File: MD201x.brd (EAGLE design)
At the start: 80 x 50 mm, 103 parts, among them IC1 78L05F, IC2 LM321MF, J1 8P8C-LED, J10 1744446-4, J2 1744446-4, J3 XH-4-SIDE, J4 MA04-2, J5 MA05-2, J6 MA02-2, Q1 N-MOSFET-, Q2 N-MOSFET-, Q3 N-MOSFET-, Q4 N-MOSFET-, U1 STM32F103C8, U10 XC6206, U11 74AHC1G08DCK, U12 74AHC1G08DCK, U13 74AHC1G08DCK, U14 74AHC1G08DCK, U15 74AHC1G08DCK, U2 NCV7351D1E, U3 SI8621AB-B-IS, U4 TLP184, U5 NCP5106D, U6 NCP5106D, U7 NCS199, U8 7815DT, U9 7805DT, X1 CSTCE8M00G55

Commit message: 横向き
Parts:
- removed C35: 22u, rcl:E2,5-5
- removed U11, U12, U13, U14, U15: 74AHC1G08DCK, 74xx-little-us:SC70-5
- added D2, D3, D5, D6: (no value), diode:SOD523
- added Q5: BSS123, transistor-small-signal:SOT23
- added R19: 0.5m, r_shunt:CSS2H-2512
- C33: device rcl:C0805 -> rcl:C0603
- C36: device rcl:C0603 -> rcl:C1210
- U$1: value XT60PW -> XT60PW-M; device lib_ysk:XT60PW-F -> lib_ysk:XT60PW-M
- U$2: value XT60PW -> XT60PW-F
- moved R17 101.6 mm to (20.1, 47.5), flipped to the bottom
- moved R18 94.9 mm to (20.1, 34.8), flipped to the bottom
- moved D1 43.1 mm to (62.4, -2.26), turned to 270 degrees
- moved C15 40.8 mm to (34.1, 46.1)
- moved U7 36.5 mm to (45.0, 44.5), flipped to the top, turned to 270 degrees
- moved C27 36.3 mm to (34.0, -4.16), turned to 90 degrees
- moved C28 33.0 mm to (40.4, -3.50), turned to 90 degrees
- moved C11 32.4 mm to (48.3, 8.88), flipped to the bottom, turned to 0 degrees
- moved C13 31.2 mm to (50.2, 7.51), flipped to the top, turned to 0 degrees
- moved R3 28.6 mm to (68.8, 41.9)
- moved C5 27.5 mm to (49.7, 11.9), flipped to the bottom, turned to 0 degrees
- moved D4 25.9 mm to (59.3, -2.70), turned to 270 degrees
- moved R5 24.7 mm to (68.2, 43.9)
- moved C36 24.6 mm to (14.1, 42.1), flipped to the bottom, turned to 180 degrees
- moved IC1 24.4 mm to (14.6, 46.8), flipped to the bottom, turned to 90 degrees
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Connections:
- net N$23 renamed CANTX_ISO
- net N$27 renamed CANRX_ISO
- net VCS_N renamed VCS_B_N
- net VCS_P renamed VCS_B_P
- removed net 24V_ISO: C35.+, C36.1, IC1.3, J1.4, J1.5, R20.1
- removed net VCS: C11.2, C12.2, C5.2, C6.2, Q2.1, Q2.2, Q2.3, Q4.1, Q4.2, Q4.3, R7.1, R8.1, R9.2$1, R9.2$2
- new net A_LS: Q2.1, Q2.2, Q2.3, R19.2, R7.1
- new net B_LS: C6.2, Q4.1, Q4.2, Q4.3, R8.1, R9.2
- new net DC_ISO: C36.1, IC1.3, J1.4, J1.5, R20.1
- new net ISENSE_B: C16.2, R123.1
- new net N$13: J6.1
- net !EMS: no longer U12.1, U13.1, U14.1, U15.1
- net +3V3: no longer U12.5, U13.5, U14.5, U15.5
- net 5V_ISO: now also R17.2; no longer U11.5
- net CANH: no longer J6.1
- net CANL: no longer R12.1
- net GNDA: now also C11.2, C12.2, C5.2, R19.1, R9.1; no longer R9.1$1, R9.1$2, U12.3, U13.3, U14.3, U15.3
- net GNDIO: now also Q5.2; no longer C35.-, R17.1, U11.3
- net IN_HI_A: no longer U13.4
- net IN_HI_A_PRE: no longer U13.2
- net IN_HI_B: no longer U14.4
- net IN_HI_B_PRE: no longer U14.2
- net IN_LO_A: no longer U12.4
- net IN_LO_A_PRE: no longer U12.2
- net IN_LO_B: no longer U15.4
- net IN_LO_B_PRE: no longer U15.2
- net ISENSE: no longer C16.2, R123.1
- net N$1: now also D6.C
- net N$11: now also D5.C
- net N$12: now also D2.A
- net N$16: now also R17.1; no longer U11.4
- net N$17: now also Q5.3; no longer R17.2
- net N$2: now also D2.C
- net N$4: now also D6.A
- net N$5: now also D3.C
- net N$61: now also D5.A
- net N$64: now also D3.A
- net N$8: now also Q5.1; no longer U11.1, U11.2
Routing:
- net +3V3: track 85.9 -> 34.6 mm, vias 6 -> 2
- net DC_ISO: track 0.00 -> 27.6 mm, vias 0 -> 2
- net SWDIO: track 29.5 -> 4.91 mm, vias 1 -> 0
- net SWCLK: track 23.6 -> 5.09 mm, vias 1 -> 0
- net 3V3A: track 25.9 -> 7.83 mm
- net 24V_ISO: track 17.4 -> 0.00 mm
- net UART_TX: track 18.3 -> 2.51 mm, vias 1 -> 0
- net UART_RX: track 20.3 -> 4.73 mm, vias 1 -> 0
- net N$67: track 14.8 -> 0.00 mm
- net N$5: track 13.2 -> 0.00 mm, vias 1 -> 0
- net B_OUT: track 28.4 -> 15.8 mm, vias 1 -> 0
- net !EMS: track 25.7 -> 16.8 mm, vias 2 -> 1
- net N$2: track 11.6 -> 2.94 mm, vias 1 -> 0
- net N$17: track 0.00 -> 7.31 mm
- net N$64: track 5.50 -> 0.00 mm
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- added copper zone on layer 16, net A_LS
- added copper zone on layer 16, net B_LS
- added copper zone on layer 16, net B_OUT
- removed copper zone on layer 1, net A_OUT
- removed copper zone on layer 1, net B_OUT
- removed copper zone on layer 1, net VCS
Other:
- board text removed: "0"
- board text removed: "1"
- board text removed: "2"
- board text removed: "3"
- board text removed: "4"
- board text removed: "CAN TERM."
- board text removed: "OPEN"
- board text removed: "TERM"

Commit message: staging everything i have right now
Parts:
- removed U7: NCS199, on-semi:SOT65P210X110-6
- added C31: (no value), rcl:C0603
- added CN2: (no value), jst-xa:S3B-XASK-1
- added R22, R23: 10, rcl:R0603
- added U$3: INA186DCK, lib_ysk:SOT65P210X110-6
- U5: value NCP5106D -> NCP5106MN; device on-semi:SOIC127P600X175-8 -> on-semi:SON80P400X400X100-11T275X300
- U6: value NCP5106D -> NCP5106; device on-semi:SOIC127P600X175-8 -> on-semi:SO08
- moved D5 122.4 mm to (50.4, 20.3), flipped to the bottom, turned to 180 degrees
- moved D3 121.2 mm to (40.7, 32.6), turned to 90 degrees
- moved CN1 74.5 mm to (16.4, 9.40), turned to 180 degrees
- moved D6 62.7 mm to (-7.40, -11.7)
- moved R7 42.4 mm to (40.9, 12.4)
- moved D4 40.5 mm to (34.4, 29.3), flipped to the top, turned to 180 degrees
- moved U5 38.0 mm to (39.6, 11.9), flipped to the top, turned to 0 degrees
- moved J2 32.3 mm to (48.7, -16.1)
- moved C1 32.0 mm to (58.4, 43.8), turned to 90 degrees
- moved C22 31.9 mm to (-14.8, 19.9)
- moved C2 30.9 mm to (48.0, 43.8), turned to 90 degrees
- moved R3 29.7 mm to (50.5, 18.5)
- moved S1 27.3 mm to (-10.0, 16.3)
- moved R6 26.8 mm to (42.0, 23.0), turned to 90 degrees
- moved J10 18.2 mm to (4.50, -4.40)
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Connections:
- new net 0V: C11.2, C12.2, C5.2, R19.1, R9.1
- new net N$15: C31.2, R22.2, U$3.5
- new net N$22: C31.1, R23.2, U$3.4
- net 3V3A: now also U$3.3; no longer U7.3
- net GNDA: now also U$3.2; no longer C11.2, C12.2, C5.2, R19.1, R9.1, U7.2
- net N$1: now also U5.8; no longer U5.7
- net N$6: no longer U7.6
- net N$73: now also U5.10; no longer U5.8
- net REF: no longer U7.1
- net VCS_B_N: now also R22.1; no longer U7.5
- net VCS_B_P: now also R23.1; no longer U7.4
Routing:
- net +5V: track 40.8 -> 30.3 mm
- net N$11: track 0.00 -> 10.3 mm
- net !RESET: track 14.7 -> 5.97 mm, vias 1 -> 0
- net N$64: track 0.00 -> 7.88 mm
- net N$12: track 9.49 -> 15.4 mm
- net DC_ISO: track 27.6 -> 22.0 mm
- net SWCLK: track 5.09 -> 0.00 mm
- net SWDIO: track 4.91 -> 0.00 mm
- net UART_RX: track 4.73 -> 0.00 mm
- net N$61: track 0.00 -> 3.76 mm
- net VCS_B_N: track 0.00 -> 3.68 mm
- net +3V3: track 34.6 -> 31.0 mm
- net N$2: track 2.94 -> 0.00 mm
- net !EMS_ISO: track 9.58 -> 6.65 mm
- net UART_TX: track 2.51 -> 0.00 mm
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- added copper zone on layer 1, net 0V
- added copper zone on layer 16, net 0V

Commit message: idk
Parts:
- removed J10, J2: 1744446-4, con-ep25:1744446-4
- removed J3: XH-4-SIDE, con-xh:CON-XH-4-SIDE
- moved C31 3.44 mm to (41.6, 28.3), turned to 180 degrees
- moved R23 1.94 mm to (40.6, 30.9), turned to 270 degrees
- moved R22 1.12 mm to (42.7, 30.9), turned to 270 degrees
- moved U$3 1.08 mm to (38.1, 30.4), turned to 270 degrees
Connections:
- new net CS_OUT_A: U$3.6
- new net CS_REF: U$3.1
- net +5V: no longer J10.P2, J3.P$2
- net ENC_A: no longer J10.P3
- net ENC_B: no longer J10.P4
- net GNDA: no longer J10.P1, J3.P$1
- net IN_A: no longer J3.P$3
- net IN_B: no longer J3.P$4
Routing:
- net VCS_B_P: track 7.89 -> 10.4 mm
- net N$15: track 0.00 -> 1.85 mm
- net N$22: track 0.00 -> 1.81 mm
- net VCS_B_N: track 3.68 -> 2.56 mm

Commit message: stage everything
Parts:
- removed D4: BAS16W, diode:SOD323-R
- removed U6: NCP5106, on-semi:SO08
- added U$4: DGD05473FN, lib_ysk:SON50P300X300X80-11T165X260
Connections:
- net +15V: now also U$4.1; no longer D4.A, U6.1
- net B_OUT: now also U$4.5; no longer U6.6
- net GNDA: now also U$4.11, U$4.9; no longer U6.4
- net IN_HI_B: now also U$4.7; no longer U6.2
- net IN_LO_B: now also U$4.8; no longer U6.3
- net N$2: now also U$4.4; no longer U6.7
- net N$5: now also U$4.10; no longer U6.5
- net N$67: now also U$4.3; no longer D4.C, U6.8
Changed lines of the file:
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@@
 <attribute name="NAME" x="59.61" y="31.727" size="1.27" layer="26" font="vector" rot="MR90"/>
-</element>
-<element name="D4" library="diode" library_urn="urn:adsk.eagle:library:210" package="SOD323-R" package3d_urn="urn:adsk.eagle:package:43437/1" value="BAS16W" x="34.4" y="29.3" smashed="yes" rot="R180">
-<attribute name="NAME" x="34.151" y="28.121" size="1.27" layer="25" font="vector" rot="R90"/>
 </element>
 <element name="C10" library="rcl" package="C0603" value="100n/25V" x="34.4" y="26.9" smashed="yes">
@@
 <attribute name="VALUE" x="43.537" y="9.995" size="1.27" layer="27" rot="R90"/>
 </element>
-<element name="U6" library="on-semi" package="SO08" package3d_urn="urn:adsk.eagle:package:15356/1" value="NCP5106" x="39.4" y="25.3" smashed="yes" rot="R270">
-<attribute name="NAME" x="36.997" y="26.29" size="1.27" layer="25" font="vector" rot="SR270"/>
-<attribute name="VALUE" x="37.495" y="21.363" size="1.27" layer="27"/>
-</element>
 <element name="R9" library="r_shunt" package="CSS2H-2512" value="0.5m" x="47.8" y="30.6" smashed="yes" rot="MR180">
 <attribute name="NAME" x="46.449" y="31.122" size="1.27" layer="26" font="vector" rot="SMR180"/>
@@
 <attribute name="SPICEPREFIX" value="C" x="41.6" y="28.3" size="1.778" layer="28" rot="MR180" display="off"/>
 <attribute name="VALUE" x="40.965" y="30.205" size="1.27" layer="28" rot="MR180"/>
+</element>
+<element name="U$4" library="lib_ysk" package="SON50P300X300X80-11T165X260" package3d_urn="urn:adsk.eagle:package:12826382/1" value="DGD05473FN" x="41.7" y="27" smashed="yes">
+<attribute name="NAME" x="41.7" y="29.521" size="1.27" layer="25" align="bottom-center"/>
+<attribute name="VALUE" x="41.7" y="24.751" size="1.27" layer="27" align="top-center"/>
 </element>
 </elements>
@@
 <signal name="+15V">
 <contactref element="D1" pad="A"/>
-<contactref element="D4" pad="A"/>
-<contactref element="U6" pad="1"/>
 <contactref element="U5" pad="1"/>
 <contactref element="C7" pad="1"/>
@@
 <contactref element="U9" pad="1"/>
 <contactref element="C13" pad="1"/>
+<contactref element="U$4" pad="1"/>
 <wire x1="45.208" y1="56.034" x2="44.222" y2="59.569" width="0" layer="19" extent="1-1"/>
 <wire x1="37.82" y1="58.426" x2="44.222" y2="59.569" width="0" layer="19" extent="1-1"/>
 <wire x1="35.639" y1="33.173" x2="45.208" y2="56.034" width="0" layer="19" extent="16-16"/>
-<wire x1="33.3" y1="29.3" x2="35.639" y2="33.173" width="0" layer="19" extent="1-16"/>
-<wire x1="37.05" y1="27.205" x2="33.3" y2="29.3" width="0" layer="19" extent="1-1"/>
-<wire x1="37.64" y1="13.5" x2="37.05" y2="27.205" width="0" layer="19" extent="1-1"/>
+<wire x1="40.2654" y1="28" x2="35.639" y2="33.173" width="0" layer="19" extent="1-16"/>
+<wire x1="37.64" y1="13.5" x2="40.2654" y2="28" width="0" layer="19" extent="1-1"/>
 <wire x1="35" y1="13.05" x2="37.64" y2="13.5" width="0" layer="19" extent="1-16"/>
 <wire x1="46.278" y1="4.306" x2="37.64" y2="13.5" width="0" layer="19" extent="1-1"/>
@@
 <contactref element="U5" pad="4"/>
 <contactref element="C7" pad="2"/>
-<contactref element="U6" pad="4"/>
 <contactref element="C8" pad="2"/>
 <contactref element="U3" pad="4"/>
@@
 <contactref element="U$1" pad="NEG"/>
 <contactref element="U$3" pad="2"/>
+<contactref element="U$4" pad="9"/>
+<contactref element="U$4" pad="11"/>
 <wire x1="42.668" y1="56.034" x2="51.522" y2="61.849" width="0" layer="19" extent="1-1"/>
 <wire x1="33.818" y1="54.231" x2="42.668" y2="56.034" width="0" layer="19" extent="1-1"/>
@@
 <contactref element="Q3" pad="1"/>
 <contactref element="Q3" pad="2"/>
-<contactref element="U6" pad="6"/>
 <contactref element="R6" pad="1"/>
 <polygon width="0.1524" layer="16" thermals="no" rank="3">
@@
 <wire x1="44.1" y1="22.8" x2="43.3" y2="22" width="0.254" layer="16"/>
 <wire x1="49" y1="22.8" x2="44.1" y2="22.8" width="0.254" layer="16"/>
+<contactref element="U$4" pad="5"/>
 <wire x1="58.825" y1="27.505" x2="56.8" y2="31.6" width="0" layer="19" extent="16-16"/>
 <wire x1="42" y1="22.15" x2="43.3" y2="22" width="0" layer="19" extent="16-16"/>
-<wire x1="41.75" y1="24.665" x2="42" y2="22.15" width="0" layer="19" extent="1-16"/>
-<wire x1="35.25" y1="26.9" x2="41.75" y2="24.665" width="0" layer="19" extent="1-1"/>
+<wire x1="40.2654" y1="26" x2="42" y2="22.15" width="0" layer="19" extent="1-16"/>
+<wire x1="35.25" y1="26.9" x2="40.2654" y2="26" width="0" layer="19" extent="1-1"/>
 <wire x1="64" y1="13.4" x2="56.7" y2="22.2" width="0" layer="19" extent="16-16"/>
 </signal>
 <signal name="N$67">
-<contactref element="D4" pad="C"/>
 <contactref element="C10" pad="1"/>
-<contactref element="U6" pad="8"/>
-<wire x1="35.5" y1="29.3" x2="41.75" y2="27.205" width="0" layer="19" extent="1-1"/>
-<wire x1="33.55" y1="26.9" x2="35.5" y2="29.3" width="0" layer="19" extent="1-1"/>
+<contactref element="U$4" pad="3"/>
+<wire x1="33.55" y1="26.9" x2="40.2654" y2="27" width="0" layer="19" extent="1-1"/>
 </signal>
 <signal name="A_OUT">
@@
 <contactref element="R4" pad="1"/>
 <contactref element="R8" pad="2"/>
-<contactref element="U6" pad="5"/>
 <contactref element="D3" pad="C"/>
+<contactref element="U$4" pad="10"/>
 <wire x1="40.7" y1="32" x2="40.95" y2="35.3" width="0" layer="19" extent="1-1"/>
 <wire x1="42.4" y1="31.75" x2="40.7" y2="32" width="0" layer="19" extent="1-1"/>
-<wire x1="41.75" y1="23.395" x2="42.4" y2="31.75" width="0" layer="19" extent="1-1"/>
+<wire x1="43.1346" y1="28" x2="42.4" y2="31.75" width="0" layer="19" extent="1-1"/>
 </signal>
 <signal name="+3V3">
@@
 <contactref element="R2" pad="1"/>
 <contactref element="R6" pad="2"/>
-<contactref element="U6" pad="7"/>
 <contactref element="D2" pad="C"/>
-<wire x1="42" y1="23.85" x2="41.75" y2="25.935" width="0" layer="19" extent="1-16"/>
+<contactref element="U$4" pad="4"/>
 <wire x1="39.8" y1="23.85" x2="42" y2="23.85" width="0" layer="19" extent="16-16"/>
 <wire x1="37.8" y1="23.7" x2="39.8" y2="23.85" width="0" layer="19" extent="16-16"/>
+<wire x1="40.2654" y1="26.5" x2="39.8" y2="23.85" width="0" layer="19" extent="1-16"/>
 </signal>
 <signal name="CANH">
@@
 <wire x1="23.876" y1="25.312" x2="25.865" y2="45.443" width="0" layer="19" extent="16-16"/>
 <wire x1="25.306021875" y1="19.05" x2="22.225" y2="20.955" width="0" layer="19" extent="1-1"/>
-</signal>
-<signal name="IN_HI_B">
-<contactref element="U6" pad="2"/>
 </signal>
 <signal name="GNDIO">
@@
 <contactref element="U5" pad="3"/>
 </signal>
-<signal name="IN_LO_B">
-<contactref element="U6" pad="3"/>
-</signal>
 <signal name="N$6">
 <contactref element="R123" pad="2"/>
@@
 <contactref element="U$3" pad="6"/>
 </signal>
+<signal name="IN_LO_B">
+<contactref element="U$4" pad="8"/>
+</signal>
+<signal name="IN_HI_B">
+<contactref element="U$4" pad="7"/>
+</signal>
 </signals>

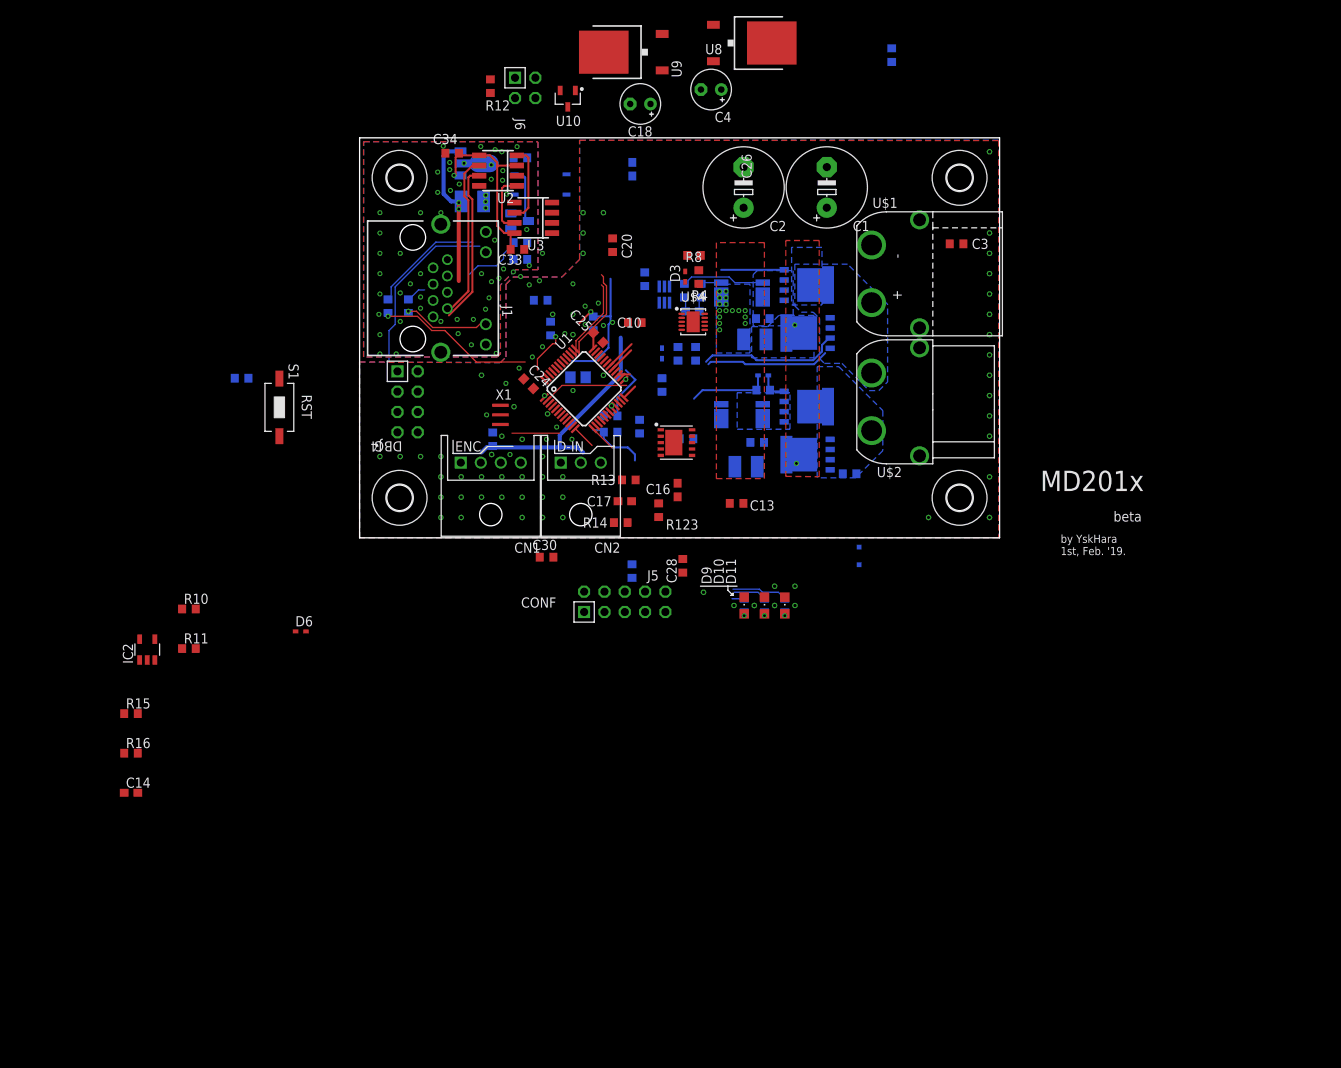
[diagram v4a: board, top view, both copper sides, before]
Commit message: change: board size to 50x100, back-to-back MOSFETs
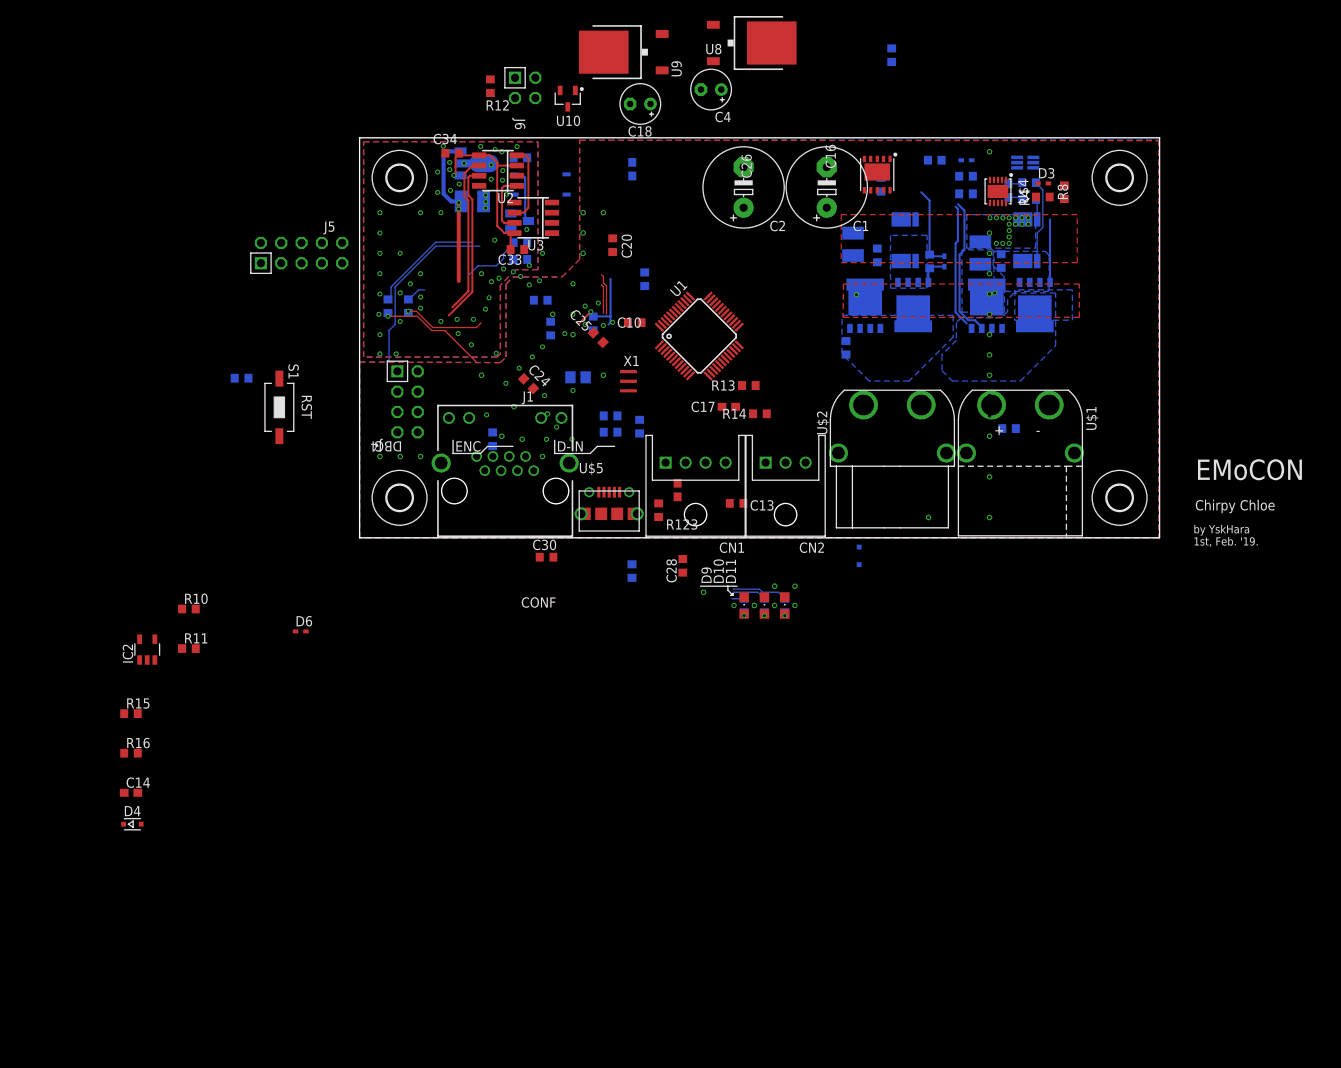
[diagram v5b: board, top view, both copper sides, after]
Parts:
- added D4: BAS16W, diode:SOD323-R
- added U$5: MICRO-USB-RECEPTACLE47589-0001, con-molex-usb:47589-0001
- U1: value STM32F103C8 -> STM32F303C
- moved J5 59.4 mm to (-7.25, 35.6)
- moved U$3 48.0 mm to (83.2, 46.9), turned to 0 degrees
- moved R8 47.0 mm to (88.1, 43.2), turned to 90 degrees
- moved D3 46.2 mm to (85.4, 44.3), turned to 0 degrees
- moved R23 45.2 mm to (83.7, 44.4), turned to 0 degrees
- moved D2 45.1 mm to (75.9, 47.2), turned to 0 degrees
- moved C9 44.2 mm to (71.9, 47.2), turned to 180 degrees
- moved R4 44.1 mm to (85.4, 42.6), turned to 0 degrees
- moved R22 42.6 mm to (83.7, 42.3), turned to 0 degrees
- moved R2 42.3 mm to (75.8, 45.2), turned to 0 degrees
- moved C31 42.3 mm to (81.1, 43.4), turned to 270 degrees
- moved U5 41.9 mm to (64.7, 45.4), turned to 270 degrees
- moved U$4 41.4 mm to (79.8, 43.3), turned to 270 degrees
- moved R7 40.0 mm to (65.2, 44.1), turned to 90 degrees
- moved R6 39.3 mm to (75.8, 43.0), turned to 180 degrees
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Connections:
- removed net IN_LO_A_PRE: U1.27
- removed net IN_LO_B_PRE: U1.26
- new net BOOT0: U1.44
- new net USB_DM: U1.32
- new net USB_DP: U1.33
- net GNDA: no longer U1.44
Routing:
- net +5V: track 30.3 -> 0.00 mm
- net +3V3: track 31.0 -> 11.7 mm
- net !EMS: track 16.8 -> 0.00 mm, vias 1 -> 0
- net 3V3A: track 7.83 -> 0.00 mm
- net CANTX: track 10.5 -> 3.66 mm
- net CANRX: track 11.8 -> 5.22 mm
- net LED_CAN: track 19.9 -> 13.8 mm
- net !RESET: track 5.97 -> 0.00 mm
- net IN_HI_A_PRE: track 3.85 -> 0.00 mm
- net IN_B: track 3.39 -> 0.00 mm
- net IN_HI_B_PRE: track 3.27 -> 0.00 mm
- net IN_A: track 2.96 -> 0.00 mm
- net IN_LO_A_PRE: track 1.46 -> 0.00 mm
- net GNDA: vias 78 -> 54
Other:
- board size 80 x 50 mm -> 100 x 50 mm
- board text added: "Chirpy Chloe"
- board text added: "EMoCON"
- board text removed: "MD201x"
- board text removed: "beta"
